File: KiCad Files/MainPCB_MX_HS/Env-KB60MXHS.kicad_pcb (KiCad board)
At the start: 2 copper layers, 283 x 126.5 mm, 153 parts, among them J1 Conn_01x04, SW1 EVQPUL, U1 Pico

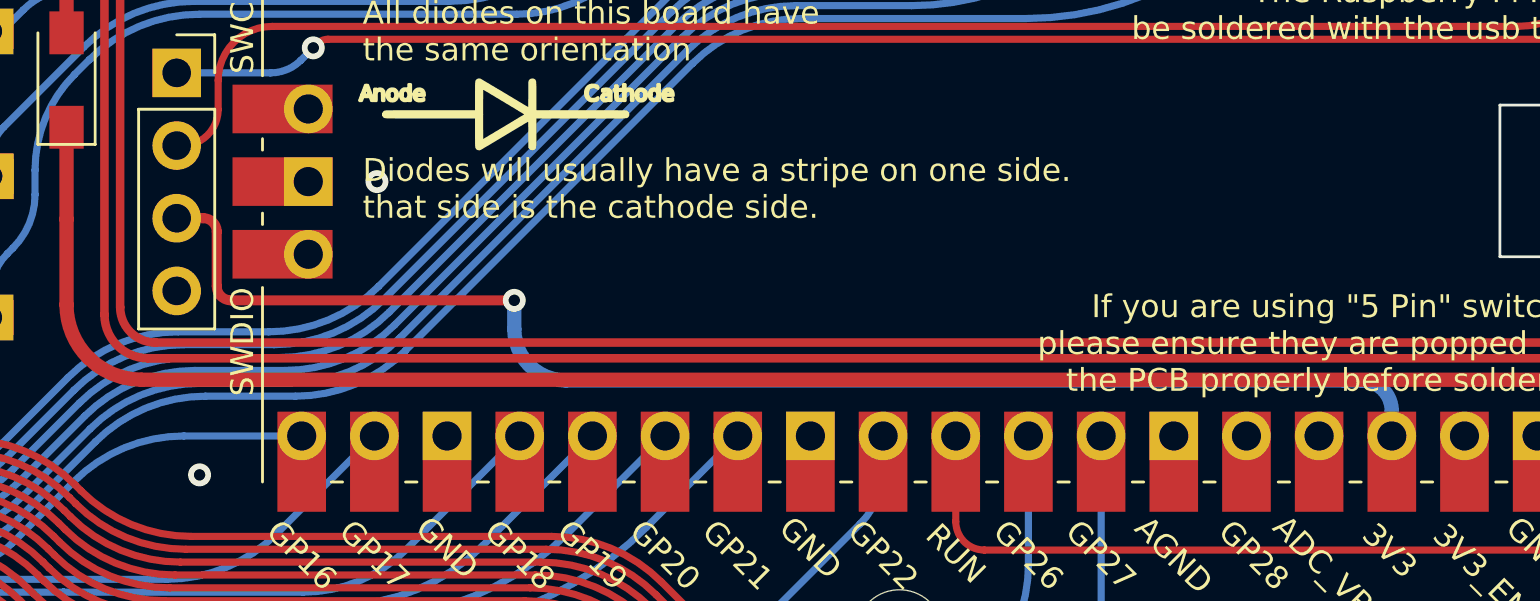
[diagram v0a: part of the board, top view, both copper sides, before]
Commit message: fixed a missing ground connection.
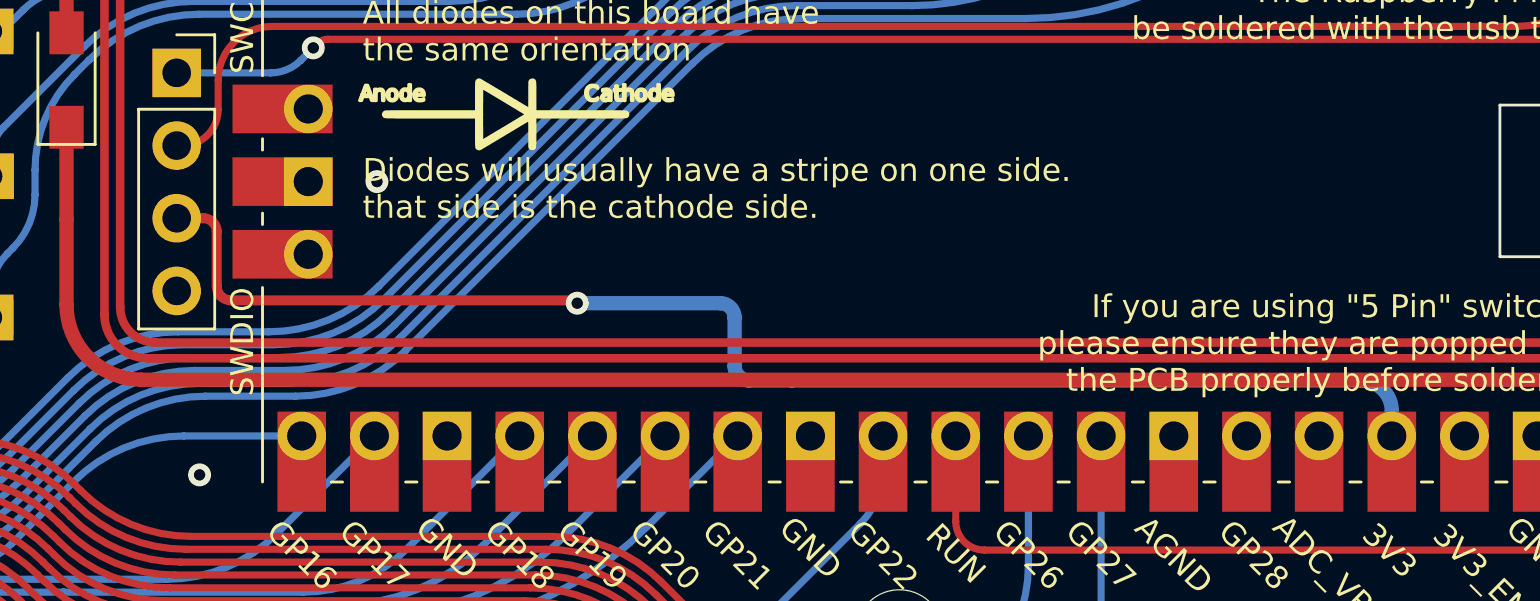
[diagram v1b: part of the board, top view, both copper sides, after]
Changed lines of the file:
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@@
 		(fp_arc
 			(start 3.80304 -1.003128)
-			(mid 3.657198 -1.03816)
+			(mid 3.657193 -1.038154)
 			(end 3.532782 -1.121938)
 			(stroke
@@
 	)
 	(segment
-		(start 305.5 53.03)
-		(end 306.433052 53.03)
+		(start 306.9 55.4)
+		(end 306.9 53.496948)
 		(width 0.35)
 		(layer "F.Cu")
@@
 	)
 	(segment
-		(start 317.3 55.9)
-		(end 307.4 55.9)
+		(start 306.433052 53.03)
+		(end 305.5 53.03)
 		(width 0.35)
 		(layer "F.Cu")
@@
 	)
 	(segment
-		(start 306.9 55.4)
-		(end 306.9 53.496948)
+		(start 319.5 56)
+		(end 319.4 55.9)
+		(width 0.35)
+		(layer "F.Cu")
+		(net 102)
+	)
+	(segment
+		(start 319.4 55.9)
+		(end 307.4 55.9)
 		(width 0.35)
 		(layer "F.Cu")
@@
 	)
 	(via
-		(at 317.3 55.9)
+		(at 319.5 56)
 		(size 0.8)
 		(drill 0.4)
@@
 	)
 	(segment
-		(start 347.97 60.64)
-		(end 347.97 59.77)
+		(start 325 58.2)
+		(end 325 56.5)
 		(width 0.5)
 		(layer "B.Cu")
@@
 	)
 	(segment
-		(start 317.3 56.9)
-		(end 317.3 55.9)
+		(start 346.9 58.7)
+		(end 327 58.7)
 		(width 0.5)
 		(layer "B.Cu")
@@
 	)
 	(segment
-		(start 346.3 58.7)
-		(end 319.1 58.7)
+		(start 324.5 56)
+		(end 319.5 56)
 		(width 0.5)
 		(layer "B.Cu")
@@
 	)
 	(segment
-		(start 346.9 58.7)
-		(end 346.3 58.7)
+		(start 347.97 60.64)
+		(end 347.97 59.77)
+		(width 0.5)
+		(layer "B.Cu")
+		(net 102)
+	)
+	(segment
+		(start 327 58.7)
+		(end 325.5 58.7)
 		(width 0.5)
 		(layer "B.Cu")
@@
 	)
 	(arc
-		(start 347.97 59.77)
-		(mid 347.656604 59.013396)
-		(end 346.9 58.7)
+		(start 324.5 56)
+		(mid 324.853553 56.146447)
+		(end 325 56.5)
 		(width 0.5)
 		(layer "B.Cu")
@@
 	)
 	(arc
-		(start 319.1 58.7)
-		(mid 317.827208 58.172792)
-		(end 317.3 56.9)
+		(start 325.5 58.7)
+		(mid 325.146447 58.553553)
+		(end 325 58.2)
+		(width 0.5)
+		(layer "B.Cu")
+		(net 102)
+	)
+	(arc
+		(start 347.97 59.77)
+		(mid 347.656604 59.013396)
+		(end 346.9 58.7)
 		(width 0.5)
 		(layer "B.Cu")

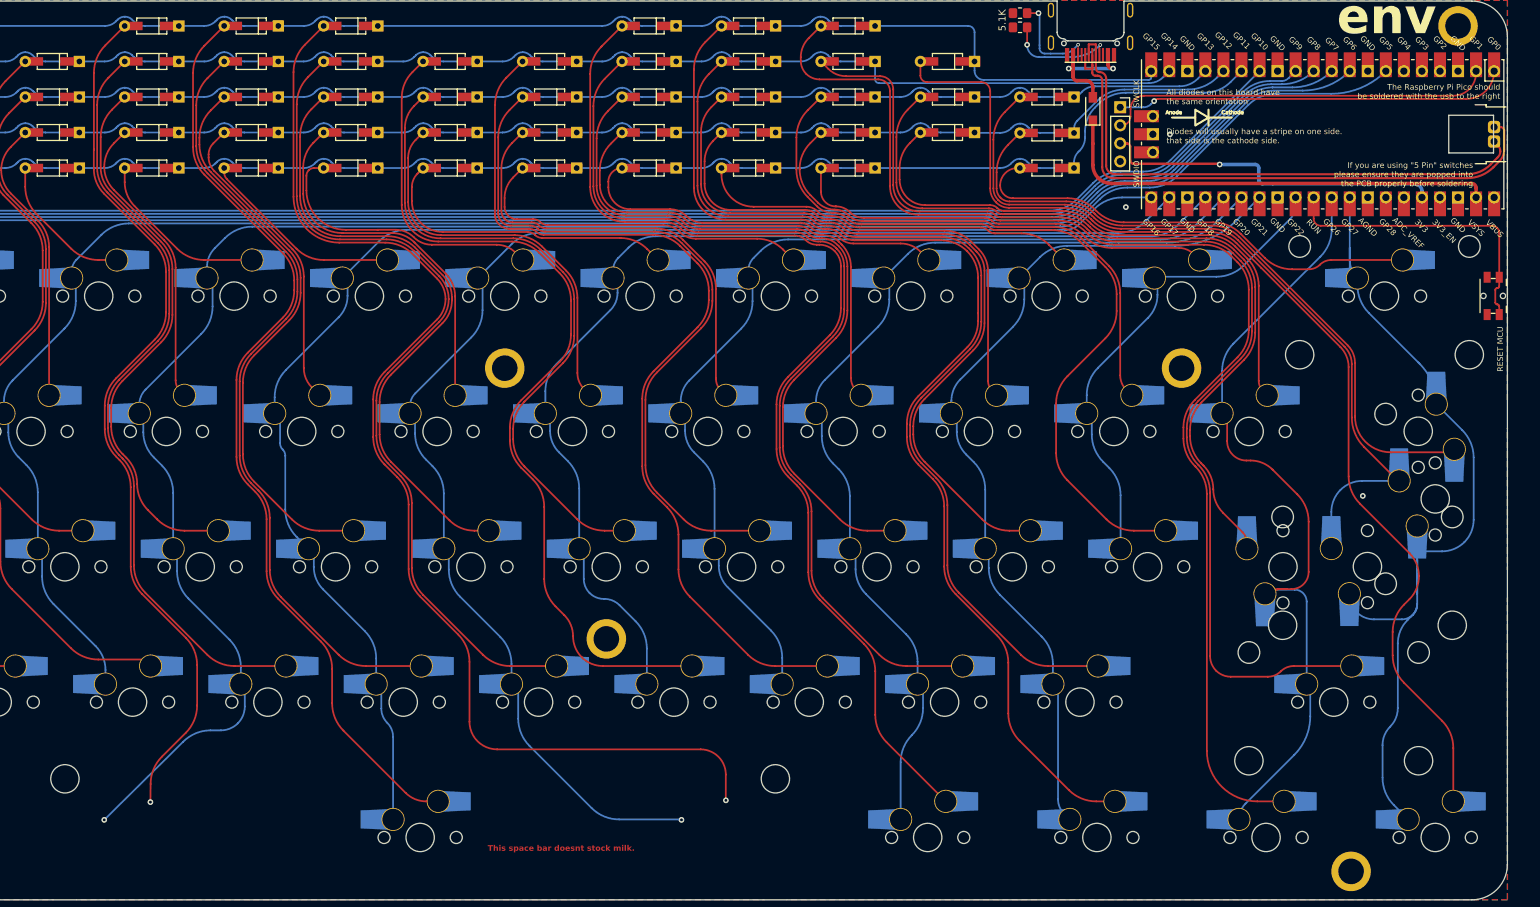
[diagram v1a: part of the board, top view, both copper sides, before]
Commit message: changed TP pad cutout for USB to be on the edge of the board for easier soldering, updated silkscreen note.
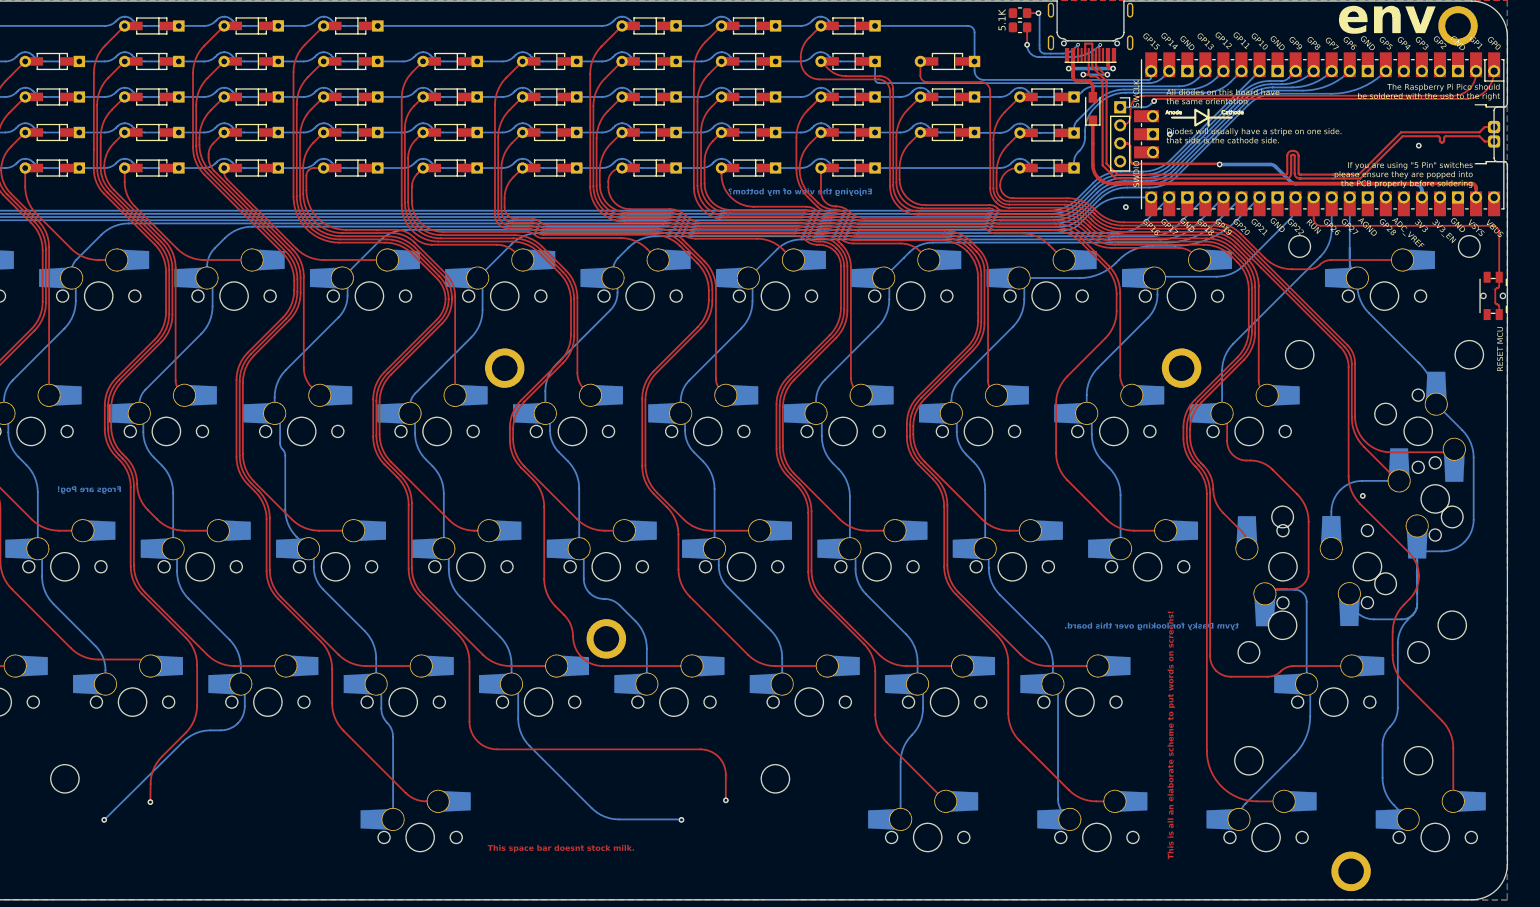
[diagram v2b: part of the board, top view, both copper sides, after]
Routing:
- net USB2_N: track 78.7 -> 90.4 mm, vias 0 -> 2
- net Net-(J1-Pin_3): track 48.6 -> 47.4 mm
- net GND: vias 4 -> 5
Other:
- outline, holes or cut-outs redrawn
- board text added: "<>< fish!"
- board text added: "Enjoying the view of my bottom?"
- board text added: "Frogs are Pog!"
- board text added: "This is all an elaborate scheme to put words on screens!"
- board text added: "tyvm Dasky for looking over this board."
- board text removed: "Soldering these pads are required for USB to work"
